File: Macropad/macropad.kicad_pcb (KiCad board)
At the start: 2 copper layers, 83 parts, among them J1 USB_B_Micro, J2 Conn_01x02, SW1 SW_Push, SW10 SW_Push, SW11 SW_Push, SW12 SW_Push, SW13 SW_Push, SW14 SW_Push, SW15 SW_Push, SW16 SW_Push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

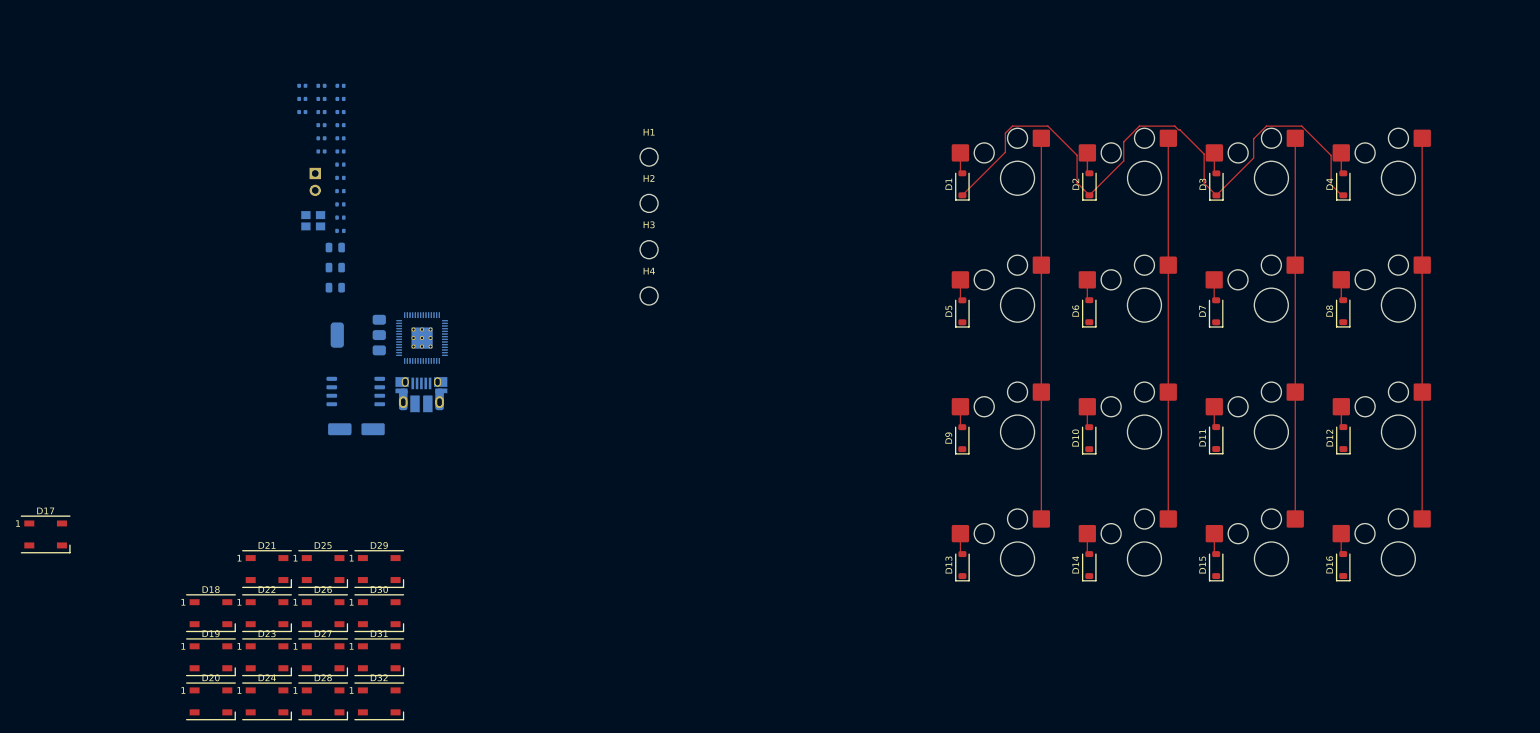
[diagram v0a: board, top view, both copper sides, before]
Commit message: macropad: Finish routing - CommsBus - Neopixels
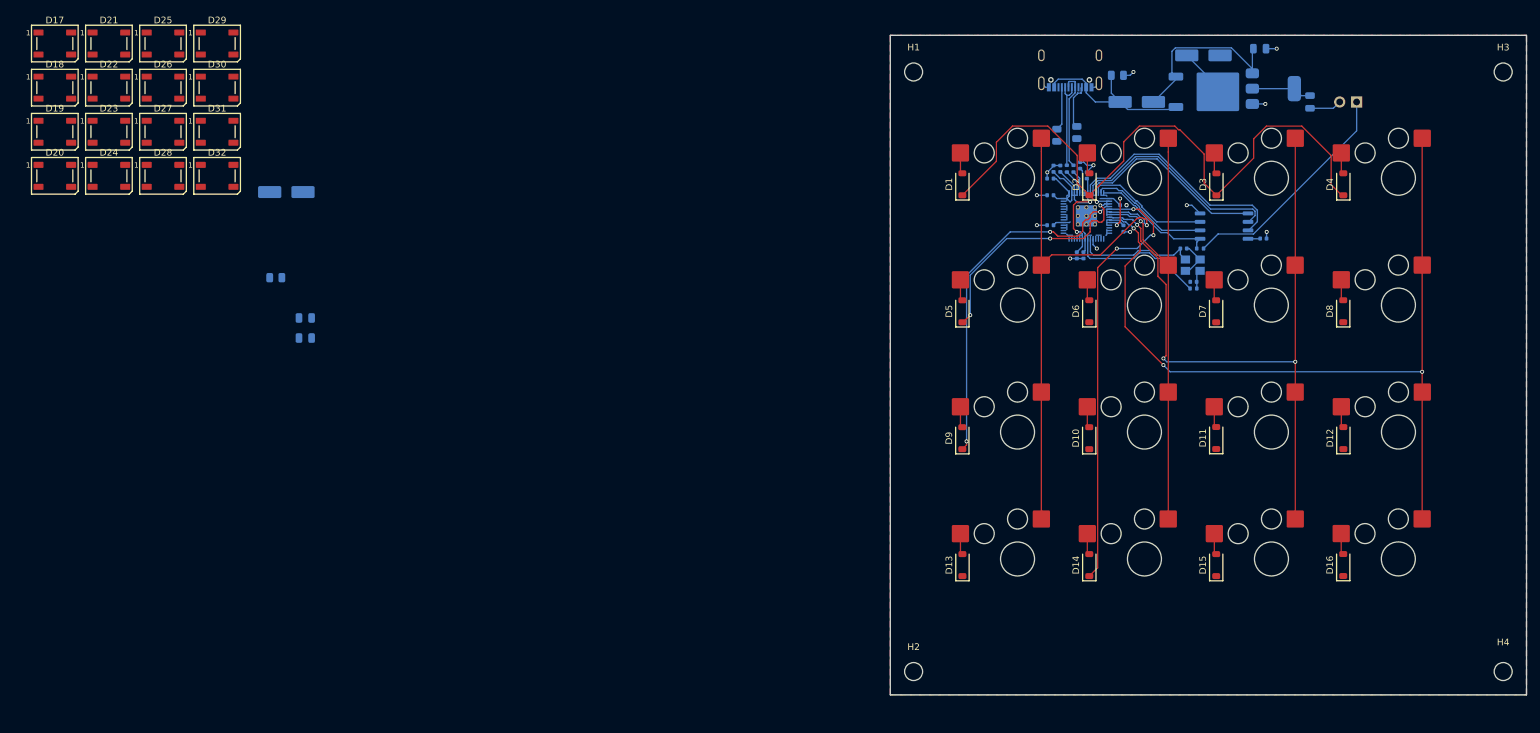
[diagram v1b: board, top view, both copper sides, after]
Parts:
- removed R2: DNF, Resistor_SMD:R_0402_1005Metric
- added D34: C8678, Diode_SMD:D_SMA_Handsoldering, B.Cu at (51.0, 21.5)
- added D35: C8678, Diode_SMD:D_SMA_Handsoldering, B.Cu at (61.0, 14.5)
- added Q1: A03401A, Package_TO_SOT_SMD:TO-252-2, B.Cu at (61.9, 20.0)
- added R7: 5.1k, Resistor_SMD:R_0805_2012Metric, B.Cu at (39.0, 26.5)
- added R8: 5.1k, Resistor_SMD:R_0805_2012Metric, B.Cu at (42.0, 26.1)
- added R9: 10k, Resistor_SMD:R_0805_2012Metric, B.Cu at (48.1, 17.5)
- C18: footprint Capacitor_SMD:C_0402_1005Metric -> Capacitor_SMD:C_0805_2012Metric
- J1: value USB_B_Micro -> USB_C_Receptacle_USB2.0_14P; footprint RP2040_minimal:USB_Micro-B_Amphenol_10103594-0001LF_Horizontal_modified -> Connector_USB:USB_C_Receptacle_G-Switch_GT-USB-7010ASV
- J2: footprint Connector_PinHeader_2.54mm:PinHeader_1x02_P2.54mm_Vertical -> Connector_PinHeader_2.54mm:PinHeader_1x02_P2.54mm_Horizontal
- R6: footprint Resistor_SMD:R_0402_1005Metric -> Resistor_SMD:R_0805_2012Metric
- U2: footprint Package_SO:SOIC-8_5.23x5.23mm_P1.27mm -> Macropad:SOIC-8_5.23x5.23mm_P1.27mm
- moved J2 156.7 mm to (84.0, 21.5), turned to 90 degrees
- moved C4 148.4 mm to (77.0, 21.5), turned to -90 degrees
- moved U1 142.3 mm to (71.5, 19.5), turned to 0 degrees
- moved C1 141.9 mm to (69.5, 13.5), turned to 0 degrees
- moved H4 140.1 mm to (106.0, 107.0)
- moved C5 139.8 mm to (70.0, 42.0), turned to 0 degrees
- moved U2 132.7 mm to (64.1, 40.1), turned to 0 degrees
- moved Y1 132.2 mm to (59.4, 46.0), turned to 0 degrees
- moved H3 131.0 mm to (106.0, 17.0)
- moved C3 130.9 mm to (59.5, 48.5)
- moved R1 129.7 mm to (60.5, 43.5), turned to 0 degrees
- moved C2 128.9 mm to (58.0, 43.5), turned to 0 degrees
- moved R5 128.5 mm to (59.5, 49.5), turned to 0 degrees
- moved C15 124.5 mm to (49.0, 37.0), turned to 0 degrees
- moved C14 120.9 mm to (49.0, 40.5), turned to -90 degrees
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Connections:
- C1 pad 1: VBUS -> +5V
- U1 pad 3: VBUS -> +5V
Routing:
- net COL3: track 57.1 -> 125.1 mm, vias 0 -> 3
- net ROW3: track 0.00 -> 67.4 mm, vias 0 -> 3
- net ROW2: track 0.00 -> 53.5 mm, vias 0 -> 3
- net COL2: track 57.1 -> 104.0 mm, vias 0 -> 3
- net +3V3: track 0.00 -> 44.2 mm, vias 0 -> 2
- net GND: track 0.00 -> 36.7 mm, vias 0 -> 13
- net ROW1: track 0.00 -> 36.0 mm, vias 0 -> 3
- net /QSPI_SD3: track 0.00 -> 35.3 mm
- net /~{USB_BOOT}: track 0.00 -> 34.6 mm
- net /QSPI_SCLK: track 0.00 -> 32.7 mm
- net /QSPI_SD0: track 0.00 -> 29.0 mm
- net +5V: track 0.00 -> 27.3 mm
- net USB5V: track 0.00 -> 26.6 mm
- net COL0: track 57.1 -> 83.6 mm, vias 0 -> 1
- net +1V1: track 0.00 -> 22.7 mm, vias 0 -> 2
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- added copper zone on B.Cu, net +3V3
- added copper zone on F.Cu, net GND
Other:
- board outline added: 95.5 x 99 mm
